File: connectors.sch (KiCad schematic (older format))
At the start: 13 parts

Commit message: Add missing pins and keep-out zone
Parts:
- removed U?: LP38693, symbol LP38693:LP38693
- added U?: LP38693, symbol LP38693:LP38693
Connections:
- net GND: now also U?.2 (GND), U?.7 (GND)
- net IN: now also U?.1 (IN), U?.6 (IN)
- net VCCOUT: now also U?.4 (OUT), U?.5 (SNS)
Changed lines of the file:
@@
 	6125 2500 6550 2500
 Connection ~ 6550 2500
+Wire Wire Line
+	6550 2050 7100 2050
+Connection ~ 6550 2050
 $Comp
 L LP38693:LP38693 U?
-U 1 1 5C7ABABC
+U 1 1 5C7B161D
 P 7500 2150
 F 0 "U?" H 7500 2515 50  0000 C CNN
@@
 	1    0    0    -1
 $EndComp
-Wire Wire Line
-	6550 2050 7100 2050
-Connection ~ 6550 2050
 $EndSCHEMATC

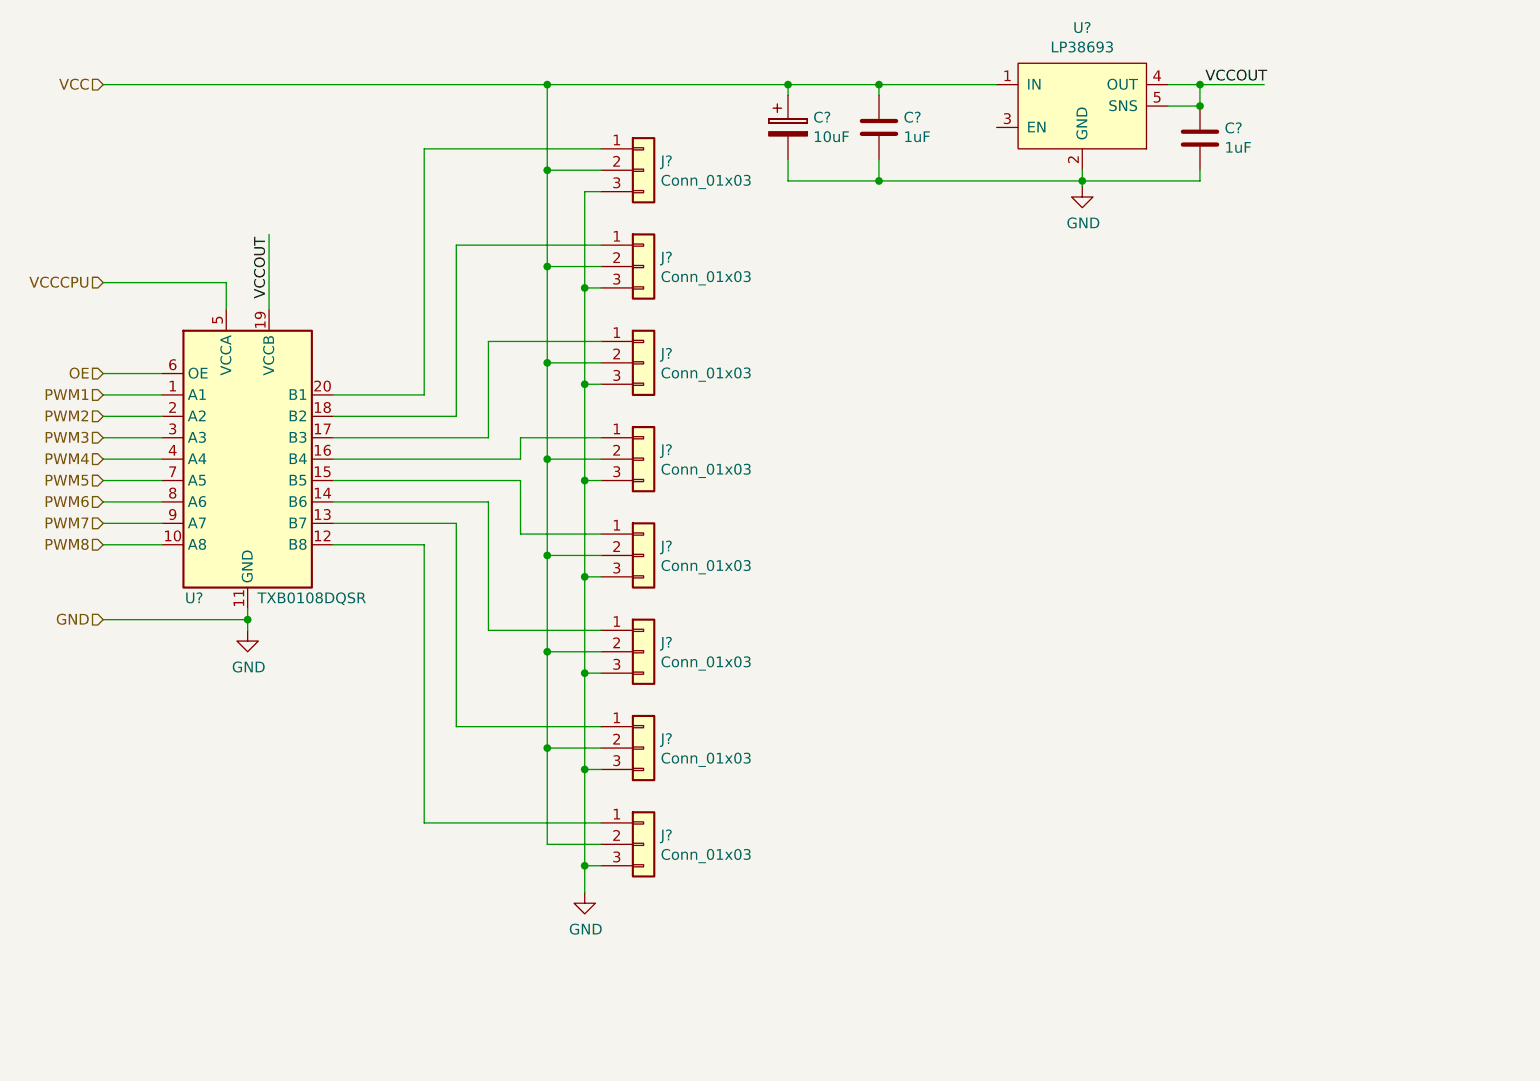
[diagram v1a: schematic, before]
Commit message: Add schema with RF modules
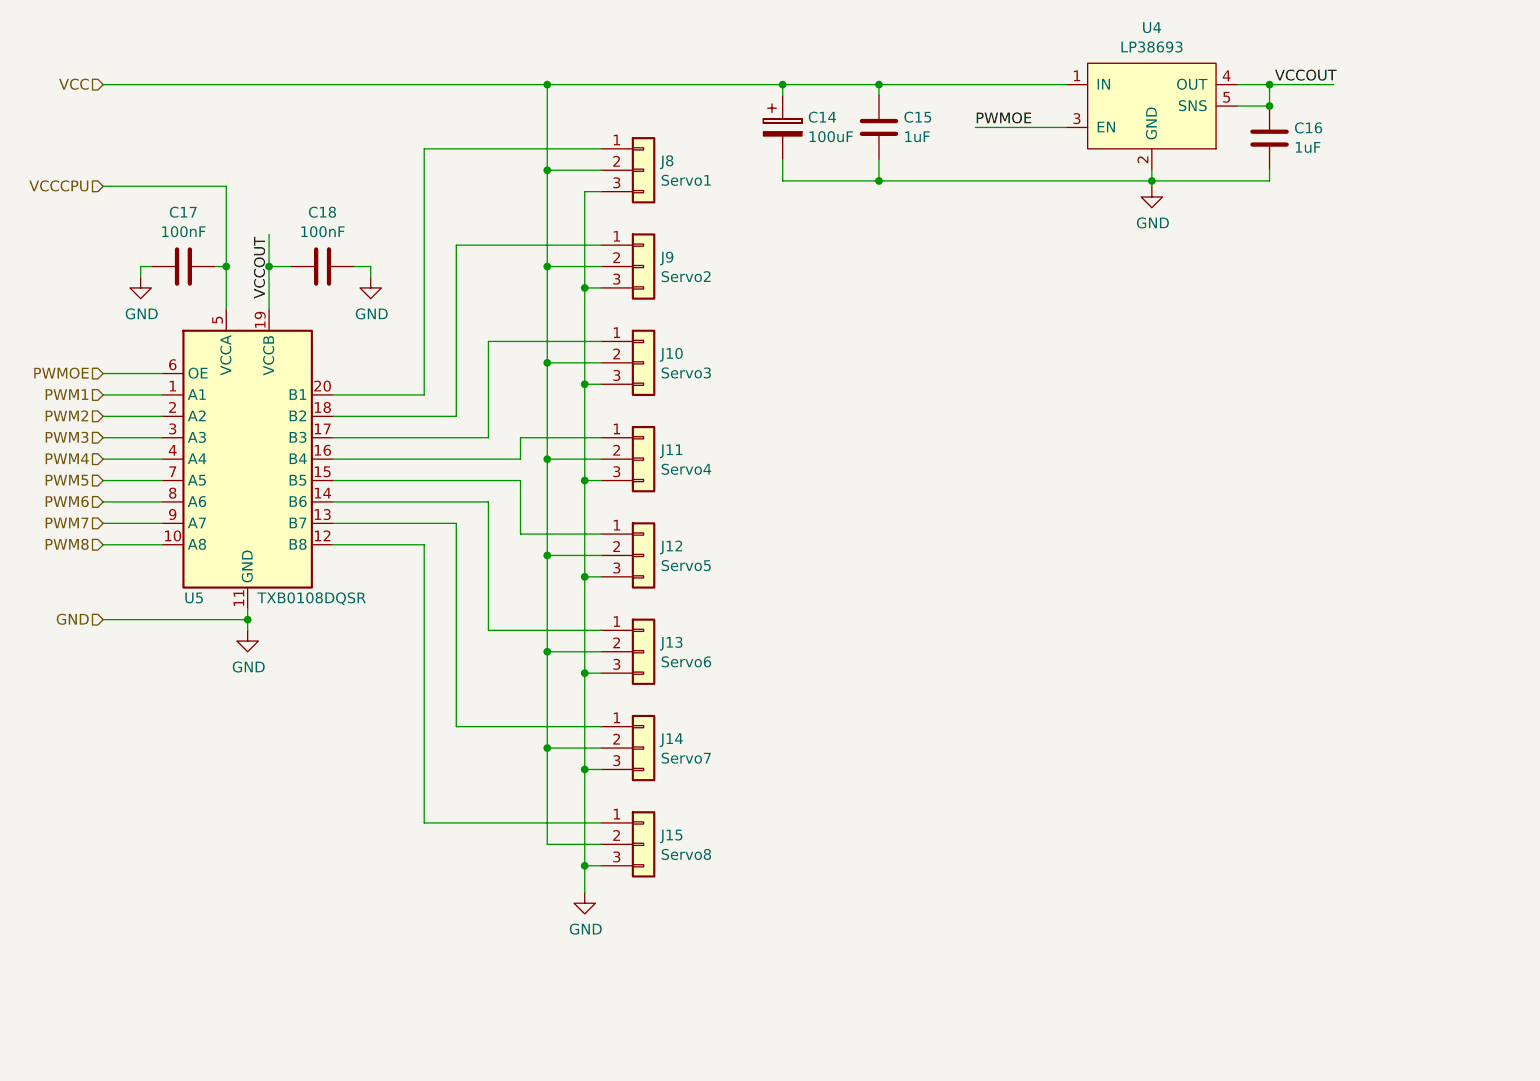
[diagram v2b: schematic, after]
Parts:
- added C17, C18: 100nF, symbol Device:C
- C14: renamed from C?; value 10uF -> 100uF
- J10: renamed from J?; value Conn_01x03 -> Servo3
- J11: renamed from J?; value Conn_01x03 -> Servo4
- J12: renamed from J?; value Conn_01x03 -> Servo5
- J13: renamed from J?; value Conn_01x03 -> Servo6
- J14: renamed from J?; value Conn_01x03 -> Servo7
- J15: renamed from J?; value Conn_01x03 -> Servo8
- J8: renamed from J?; value Conn_01x03 -> Servo1
- J9: renamed from J?; value Conn_01x03 -> Servo2
- gave numbers to parts that had none: 4
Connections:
- net OE is gone; now on net PWMOE: U5.6 (OE)
- net GND: now also C17.2, C18.1
- net VCCCPU: now also C17.1
- net VCCOUT: now also C18.2
- net PWMOE: now reaches U4.3 (EN)
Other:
- moved on the sheet: C14, C16, U4
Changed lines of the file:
@@
 $Descr A4 11693 8268
 encoding utf-8
-Sheet 2 2
+Sheet 2 3
 Title ""
 Date ""
@@
 $EndDescr
 $Comp
-L Connector_Generic:Conn_01x03 J?
+L Connector_Generic:Conn_01x03 J8
 U 1 1 5C76B44E
 P 5450 2450
-F 0 "J?" H 5530 2492 50  0000 L CNN
-F 1 "Conn_01x03" H 5530 2401 50  0000 L CNN
+F 0 "J8" H 5530 2492 50  0000 L CNN
+F 1 "Servo1" H 5530 2401 50  0000 L CNN
 F 2 "" H 5450 2450 50  0001 C CNN
 F 3 "~" H 5450 2450 50  0001 C CNN
@@
 $EndComp
 $Comp
-L Connector_Generic:Conn_01x03 J?
+L Connector_Generic:Conn_01x03 J9
 U 1 1 5C76B4B0
 P 5450 2900
-F 0 "J?" H 5530 2942 50  0000 L CNN
-F 1 "Conn_01x03" H 5530 2851 50  0000 L CNN
+F 0 "J9" H 5530 2942 50  0000 L CNN
+F 1 "Servo2" H 5530 2851 50  0000 L CNN
 F 2 "" H 5450 2900 50  0001 C CNN
 F 3 "~" H 5450 2900 50  0001 C CNN
@@
 $EndComp
 $Comp
-L Connector_Generic:Conn_01x03 J?
+L Connector_Generic:Conn_01x03 J10
 U 1 1 5C76B4D8
 P 5450 3350
-F 0 "J?" H 5530 3392 50  0000 L CNN
-F 1 "Conn_01x03" H 5530 3301 50  0000 L CNN
+F 0 "J10" H 5530 3392 50  0000 L CNN
+F 1 "Servo3" H 5530 3301 50  0000 L CNN
 F 2 "" H 5450 3350 50  0001 C CNN
 F 3 "~" H 5450 3350 50  0001 C CNN
@@
 $EndComp
 $Comp
-L Connector_Generic:Conn_01x03 J?
+L Connector_Generic:Conn_01x03 J11
 U 1 1 5C76B506
 P 5450 3800
-F 0 "J?" H 5530 3842 50  0000 L CNN
-F 1 "Conn_01x03" H 5530 3751 50  0000 L CNN
+F 0 "J11" H 5530 3842 50  0000 L CNN
+F 1 "Servo4" H 5530 3751 50  0000 L CNN
 F 2 "" H 5450 3800 50  0001 C CNN
 F 3 "~" H 5450 3800 50  0001 C CNN
@@
 $EndComp
 $Comp
-L Connector_Generic:Conn_01x03 J?
+L Connector_Generic:Conn_01x03 J12
 U 1 1 5C76B538
 P 5450 4250
-F 0 "J?" H 5530 4292 50  0000 L CNN
-F 1 "Conn_01x03" H 5530 4201 50  0000 L CNN
+F 0 "J12" H 5530 4292 50  0000 L CNN
+F 1 "Servo5" H 5530 4201 50  0000 L CNN
 F 2 "" H 5450 4250 50  0001 C CNN
 F 3 "~" H 5450 4250 50  0001 C CNN
@@
 $EndComp
 $Comp
-L Connector_Generic:Conn_01x03 J?
+L Connector_Generic:Conn_01x03 J13
 U 1 1 5C76B55C
 P 5450 4700
-F 0 "J?" H 5530 4742 50  0000 L CNN
-F 1 "Conn_01x03" H 5530 4651 50  0000 L CNN
+F 0 "J13" H 5530 4742 50  0000 L CNN
+F 1 "Servo6" H 5530 4651 50  0000 L CNN
 F 2 "" H 5450 4700 50  0001 C CNN
 F 3 "~" H 5450 4700 50  0001 C CNN
@@
 $EndComp
 $Comp
-L Connector_Generic:Conn_01x03 J?
+L Connector_Generic:Conn_01x03 J14
 U 1 1 5C76B586
 P 5450 5150
-F 0 "J?" H 5530 5192 50  0000 L CNN
-F 1 "Conn_01x03" H 5530 5101 50  0000 L CNN
+F 0 "J14" H 5530 5192 50  0000 L CNN
+F 1 "Servo7" H 5530 5101 50  0000 L CNN
 F 2 "" H 5450 5150 50  0001 C CNN
 F 3 "~" H 5450 5150 50  0001 C CNN
@@
 $EndComp
 $Comp
-L Connector_Generic:Conn_01x03 J?
+L Connector_Generic:Conn_01x03 J15
 U 1 1 5C76B5AE
 P 5450 5600
-F 0 "J?" H 5530 5642 50  0000 L CNN
-F 1 "Conn_01x03" H 5530 5551 50  0000 L CNN
+F 0 "J15" H 5530 5642 50  0000 L CNN
+F 1 "Servo8" H 5530 5551 50  0000 L CNN
 F 2 "" H 5450 5600 50  0001 C CNN
 F 3 "~" H 5450 5600 50  0001 C CNN
@@
 $EndComp
 $Comp
-L Logic_LevelTranslator:TXB0108DQSR U?
+L Logic_LevelTranslator:TXB0108DQSR U5
 U 1 1 5C76B772
 P 3600 3800
-F 0 "U?" H 3350 3150 50  0000 C CNN
+F 0 "U5" H 3350 3150 50  0000 C CNN
 F 1 "TXB0108DQSR" H 3900 3150 50  0000 C CNN
 F 2 "Package_SON:USON-20_2x4mm_P0.4mm" H 3600 3050 50  0001 C CNN
@@
 	2925 4200 3200 4200
 $Comp
-L power:GND #PWR?
+L power:GND #PWR020
 U 1 1 5C7744C7
 P 3600 4600
-F 0 "#PWR?" H 3600 4350 50  0001 C CNN
+F 0 "#PWR020" H 3600 4350 50  0001 C CNN
 F 1 "GND" H 3605 4427 50  0000 C CNN
 F 2 "" H 3600 4600 50  0001 C CNN
@@
 	3600 4600 3600 4550
 $Comp
-L power:GND #PWR?
+L power:GND #PWR021
 U 1 1 5C774AFD
 P 5175 5825
-F 0 "#PWR?" H 5175 5575 50  0001 C CNN
+F 0 "#PWR021" H 5175 5575 50  0001 C CNN
 F 1 "GND" H 5180 5652 50  0000 C CNN
 F 2 "" H 5175 5825 50  0001 C CNN
@@
 Connection ~ 5000 2450
 $Comp
-L power:GND #PWR?
+L power:GND #PWR017
 U 1 1 5C787DDB
-P 7500 2525
-F 0 "#PWR?" H 7500 2275 50  0001 C CNN
-F 1 "GND" H 7505 2352 50  0000 C CNN
-F 2 "" H 7500 2525 50  0001 C CNN
-F 3 "" H 7500 2525 50  0001 C CNN
-	1    7500 2525
-	1    0    0    -1
-$EndComp
-Wire Wire Line
-	7500 2525 7500 2500
+P 7825 2525
+F 0 "#PWR017" H 7825 2275 50  0001 C CNN
+F 1 "GND" H 7830 2352 50  0000 C CNN
+F 2 "" H 7825 2525 50  0001 C CNN
+F 3 "" H 7825 2525 50  0001 C CNN
+	1    7825 2525
+	1    0    0    -1
+$EndComp
+Wire Wire Line
+	7825 2525 7825 2500
 Connection ~ 5000 2050
 Wire Wire Line
-	7900 2050 8050 2050
-Wire Wire Line
-	8050 2050 8050 2150
-Wire Wire Line
-	8050 2150 7900 2150
-$Comp
-L Device:C C?
+	8225 2050 8375 2050
+Wire Wire Line
+	8375 2050 8375 2150
+Wire Wire Line
+	8375 2150 8225 2150
+$Comp
+L Device:C C15
 U 1 1 5C78CA1B
 P 6550 2250
-F 0 "C?" H 6665 2296 50  0000 L CNN
+F 0 "C15" H 6665 2296 50  0000 L CNN
 F 1 "1uF" H 6665 2205 50  0000 L CNN
 F 2 "" H 6588 2100 50  0001 C CNN
@@
 $EndComp
 $Comp
-L Device:C C?
+L Device:C C16
 U 1 1 5C78CA91
-P 8050 2300
-F 0 "C?" H 8165 2346 50  0000 L CNN
-F 1 "1uF" H 8165 2255 50  0000 L CNN
-F 2 "" H 8088 2150 50  0001 C CNN
-F 3 "~" H 8050 2300 50  0001 C CNN
-	1    8050 2300
-	1    0    0    -1
-$EndComp
-Connection ~ 8050 2150
-Wire Wire Line
-	7500 2500 8050 2500
-Wire Wire Line
-	8050 2500 8050 2450
-Connection ~ 7500 2500
-Wire Wire Line
-	7500 2500 7500 2450
-Wire Wire Line
-	8050 2050 8350 2050
-Connection ~ 8050 2050
-Text Label 8075 2050 0    50   ~ 0
+P 8375 2300
+F 0 "C16" H 8490 2346 50  0000 L CNN
+F 1 "1uF" H 8490 2255 50  0000 L CNN
+F 2 "" H 8413 2150 50  0001 C CNN
+F 3 "~" H 8375 2300 50  0001 C CNN
+	1    8375 2300
+	1    0    0    -1
+$EndComp
+Connection ~ 8375 2150
+Wire Wire Line
+	7825 2500 8375 2500
+Wire Wire Line
+	8375 2500 8375 2450
+Connection ~ 7825 2500
+Wire Wire Line
+	7825 2500 7825 2450
+Wire Wire Line
+	8375 2050 8675 2050
+Connection ~ 8375 2050
+Text Label 8400 2050 0    50   ~ 0
 VCCOUT
 Wire Wire Line
-	3700 3100 3700 2750
+	3700 3100 3700 2900
 Text Label 3700 3050 1    50   ~ 0
 VCCOUT
@@
 Wire Wire Line
 	6550 2400 6550 2500
-Wire Wire Line
-	6550 2500 7500 2500
 Text HLabel 2925 2050 0    50   Input ~ 0
 VCC
-Text HLabel 2925 2975 0    50   Input ~ 0
+Text HLabel 2925 2525 0    50   Input ~ 0
 VCCCPU
 Wire Wire Line
-	2925 2975 3500 2975
-Wire Wire Line
-	3500 2975 3500 3100
+	2925 2525 3500 2525
+Wire Wire Line
+	3500 2525 3500 2900
 Wire Wire Line
 	2925 2050 5000 2050
 Text HLabel 2925 3400 0    50   Input ~ 0
-OE
+PWMOE
 Text HLabel 2925 4550 0    50   Input ~ 0
 GND
@@
 	2925 3400 3200 3400
 $Comp
-L Device:CP C?
+L Device:CP C14
 U 1 1 5C79ED78
-P 6125 2250
-F 0 "C?" H 6243 2296 50  0000 L CNN
-F 1 "10uF" H 6243 2205 50  0000 L CNN
-F 2 "" H 6163 2100 50  0001 C CNN
-F 3 "~" H 6125 2250 50  0001 C CNN
-	1    6125 2250
-	1    0    0    -1
-$EndComp
-Wire Wire Line
-	6125 2100 6125 2050
-Wire Wire Line
-	5000 2050 6125 2050
-Connection ~ 6125 2050
-Wire Wire Line
-	6125 2050 6550 2050
-Wire Wire Line
-	6125 2400 6125 2500
-Wire Wire Line
-	6125 2500 6550 2500
+P 6100 2250
+F 0 "C14" H 6218 2296 50  0000 L CNN
+F 1 "100uF" H 6218 2205 50  0000 L CNN
+F 2 "" H 6138 2100 50  0001 C CNN
+F 3 "~" H 6100 2250 50  0001 C CNN
+	1    6100 2250
+	1    0    0    -1
+$EndComp
+Wire Wire Line
+	6100 2400 6100 2500
+Wire Wire Line
+	6100 2500 6550 2500
+$Comp
+L LP38693:LP38693 U4
+U 1 1 5C7B161D
+P 7825 2150
+F 0 "U4" H 7825 2515 50  0000 C CNN
+F 1 "LP38693" H 7825 2424 50  0000 C CNN
+F 2 "" H 7825 2150 50  0001 C CNN
+F 3 "http://www.ti.com/lit/ds/snvs321o/snvs321o.pdf" H 7825 2150 50  0001 C CNN
+	1    7825 2150
+	1    0    0    -1
+$EndComp
+$Comp
+L Device:C C18
+U 1 1 5C7D119D
+P 3950 2900
+F 0 "C18" V 3698 2900 50  0000 C CNN
+F 1 "100nF" V 3789 2900 50  0000 C CNN
+F 2 "" H 3988 2750 50  0001 C CNN
+F 3 "~" H 3950 2900 50  0001 C CNN
+	1    3950 2900
+	0    1    1    0
+$EndComp
+$Comp
+L power:GND #PWR019
+U 1 1 5C7D1226
+P 4175 2950
+F 0 "#PWR019" H 4175 2700 50  0001 C CNN
+F 1 "GND" H 4180 2777 50  0000 C CNN
+F 2 "" H 4175 2950 50  0001 C CNN
+F 3 "" H 4175 2950 50  0001 C CNN
+	1    4175 2950
+	1    0    0    -1
+$EndComp
+Wire Wire Line
+	3800 2900 3700 2900
+Connection ~ 3700 2900
+Wire Wire Line
+	3700 2900 3700 2750
+Wire Wire Line
+	4100 2900 4175 2900
+Wire Wire Line
+	4175 2900 4175 2950
+$Comp
+L Device:C C17
+U 1 1 5C7D7B7F
+P 3300 2900
+F 0 "C17" V 3048 2900 50  0000 C CNN
+F 1 "100nF" V 3139 2900 50  0000 C CNN
+F 2 "" H 3338 2750 50  0001 C CNN
+F 3 "~" H 3300 2900 50  0001 C CNN
+	1    3300 2900
+	0    1    1    0
+$EndComp
+$Comp
+L power:GND #PWR018
+U 1 1 5C7D7BFF
+P 3100 2950
+F 0 "#PWR018" H 3100 2700 50  0001 C CNN
+F 1 "GND" H 3105 2777 50  0000 C CNN
+F 2 "" H 3100 2950 50  0001 C CNN
+F 3 "" H 3100 2950 50  0001 C CNN
+	1    3100 2950
+	1    0    0    -1
+$EndComp
+Wire Wire Line
+	3100 2950 3100 2900
+Wire Wire Line
+	3100 2900 3150 2900
+Wire Wire Line
+	3450 2900 3500 2900
+Connection ~ 3500 2900
+Wire Wire Line
+	3500 2900 3500 3100
+Wire Wire Line
+	5000 2050 6100 2050
+Wire Wire Line
+	6100 2100 6100 2050
+Connection ~ 6100 2050
+Wire Wire Line
+	6100 2050 6550 2050
+Wire Wire Line
+	7425 2050 6550 2050
+Connection ~ 6550 2050
+Wire Wire Line
+	7825 2500 6550 2500
 Connection ~ 6550 2500
 Wire Wire Line
-	6550 2050 7100 2050
-Connection ~ 6550 2050
-$Comp
-L LP38693:LP38693 U?
-U 1 1 5C7B161D
-P 7500 2150
-F 0 "U?" H 7500 2515 50  0000 C CNN
-F 1 "LP38693" H 7500 2424 50  0000 C CNN
-F 2 "" H 7500 2150 50  0001 C CNN
-F 3 "http://www.ti.com/lit/ds/snvs321o/snvs321o.pdf" H 7500 2150 50  0001 C CNN
-	1    7500 2150
-	1    0    0    -1
-$EndComp
+	7425 2250 7000 2250
+Text Label 7000 2250 0    50   ~ 0
+PWMOE
 $EndSCHEMATC

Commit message: Small changes
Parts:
- added C18, C21, C22, C24, C25, C26, C27, C28: 470pF, symbol Device:C
- added C23: 100nF, symbol Device:C
- added J13: CAN, symbol Connector_Generic:Conn_01x03
- added R7: 470k, symbol Device:R
- added R8: 4k7, symbol Device:R
- added R9: 120R, symbol Device:R
- added U5: MCP2551, digikey-footprints:SOIC-8_W3.9mm, symbol dk_Interface-Drivers-Receivers-Transceivers:MCP2551-I_SN
- U3: renamed from U4; value LP38693 -> LP38693-5.0
- renumbered C14 to C15, C15 to C16, C16 to C17, C17 to C19, C18 to C20, J13 to J14, J14 to J15, J15 to J16, U5 to U4
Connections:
- net GND: now also C18.2, C21.2, C22.2, C23.1, C24.2, C25.2, C26.2, C27.2, C28.2, J13.3 (Pin_3), R8.2, U5.2 (VSS)
- net IN: now also R7.2
- net PWMOE: no longer U3.3 (EN)
- net VCCOUT: now also C23.2, U5.3 (VDD)
- net at J8.1 (Pin_1), U4.20 (B1): now also C18.1
- net at J9.1 (Pin_1), U4.18 (B2): now also C21.1
- net at J10.1 (Pin_1), U4.17 (B3): now also C22.1
- net at J11.1 (Pin_1), U4.16 (B4): now also C24.1
- net at J12.1 (Pin_1), U4.15 (B5): now also C25.1
- net at J14.1 (Pin_1), U4.14 (B6): now also C26.1
- net at J15.1 (Pin_1), U4.13 (B7): now also C27.1
- net at J16.1 (Pin_1), U4.12 (B8): now also C28.1
- new net: R7.1, U3.3 (EN)
- new net: J13.1 (Pin_1), R9.2, U5.6 (CANL)
- new net: J13.2 (Pin_2), R9.1, U5.7 (CANH)
- new net: R8.1, U5.8 (RS)
- new net CANRX: U5.4 (RXD)
- new net CANTX: U5.1 (TXD)
- no-connect marks 0 -> 1
